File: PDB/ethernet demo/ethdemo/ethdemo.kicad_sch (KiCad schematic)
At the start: 78 parts, among them J1 0826-1X1T-GJ-F, J2 0826-1X1T-GJ-F, Q1 CSD19538Q3AT, U1 STM32H742VGTx, U2 KSZ8863RLLI, U3 TPS23861PWR, Y1 25MHz

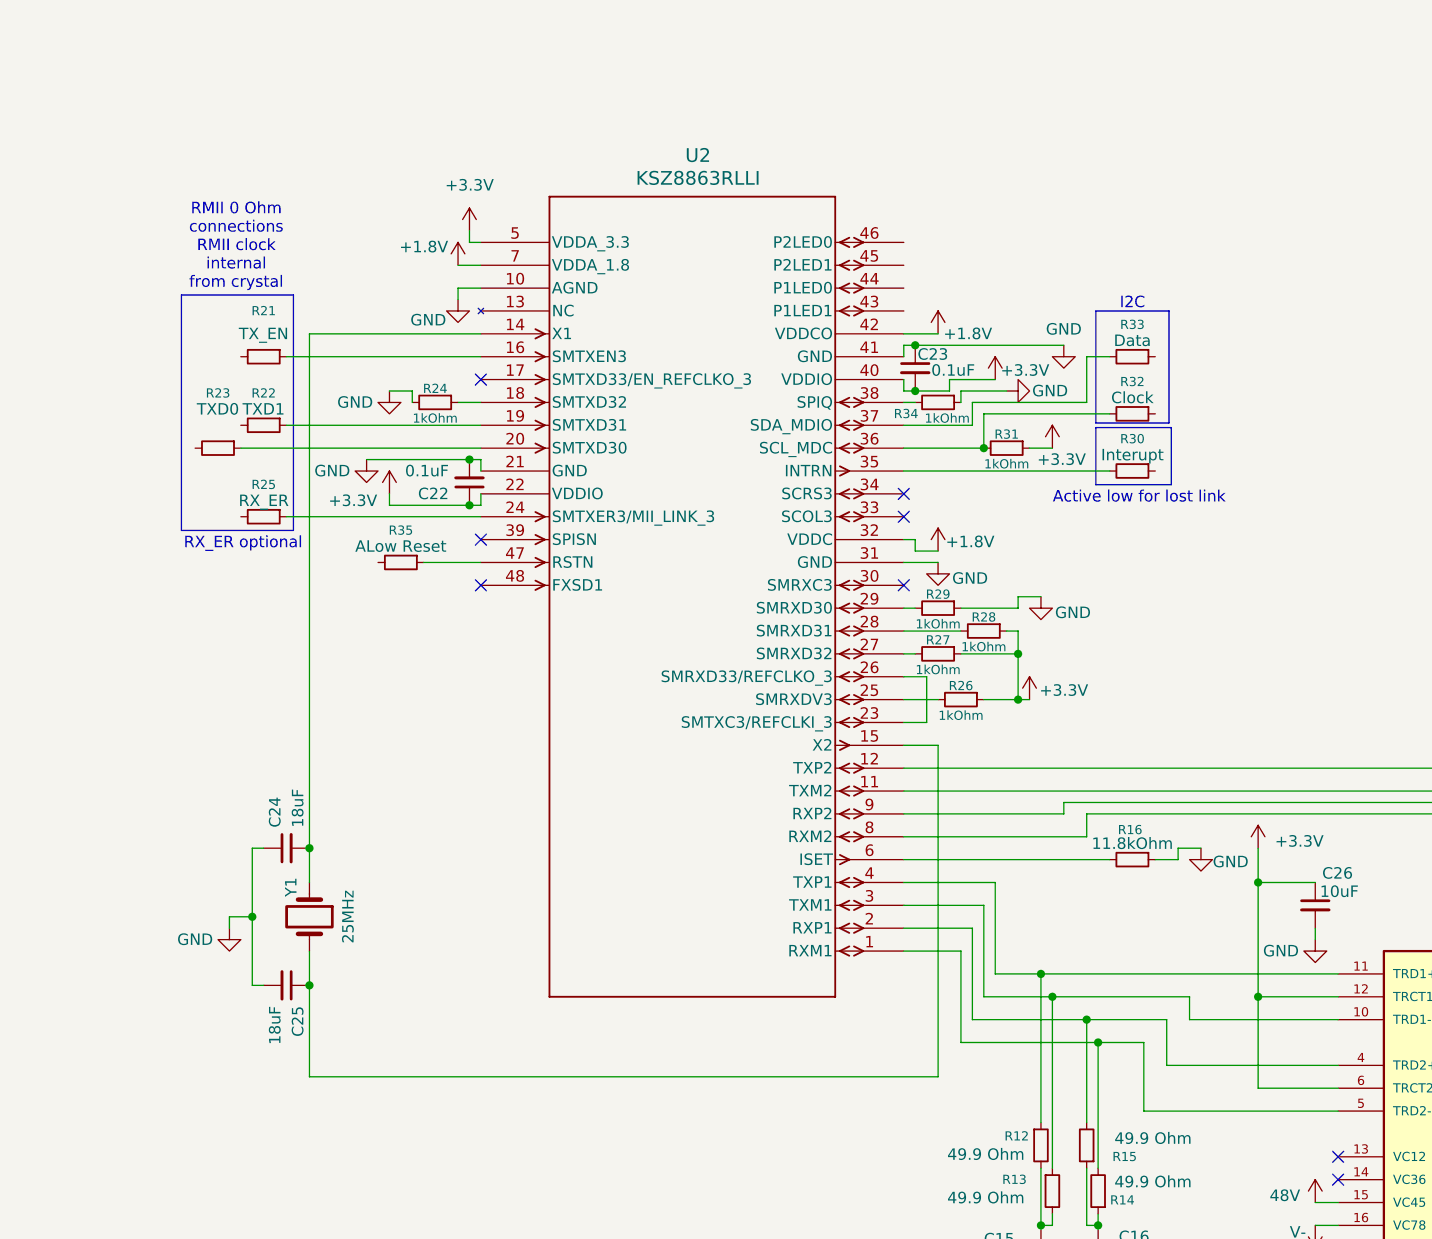
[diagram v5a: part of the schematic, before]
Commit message: Repaired Switch power
Fixed incorrect coupling for power and crystal
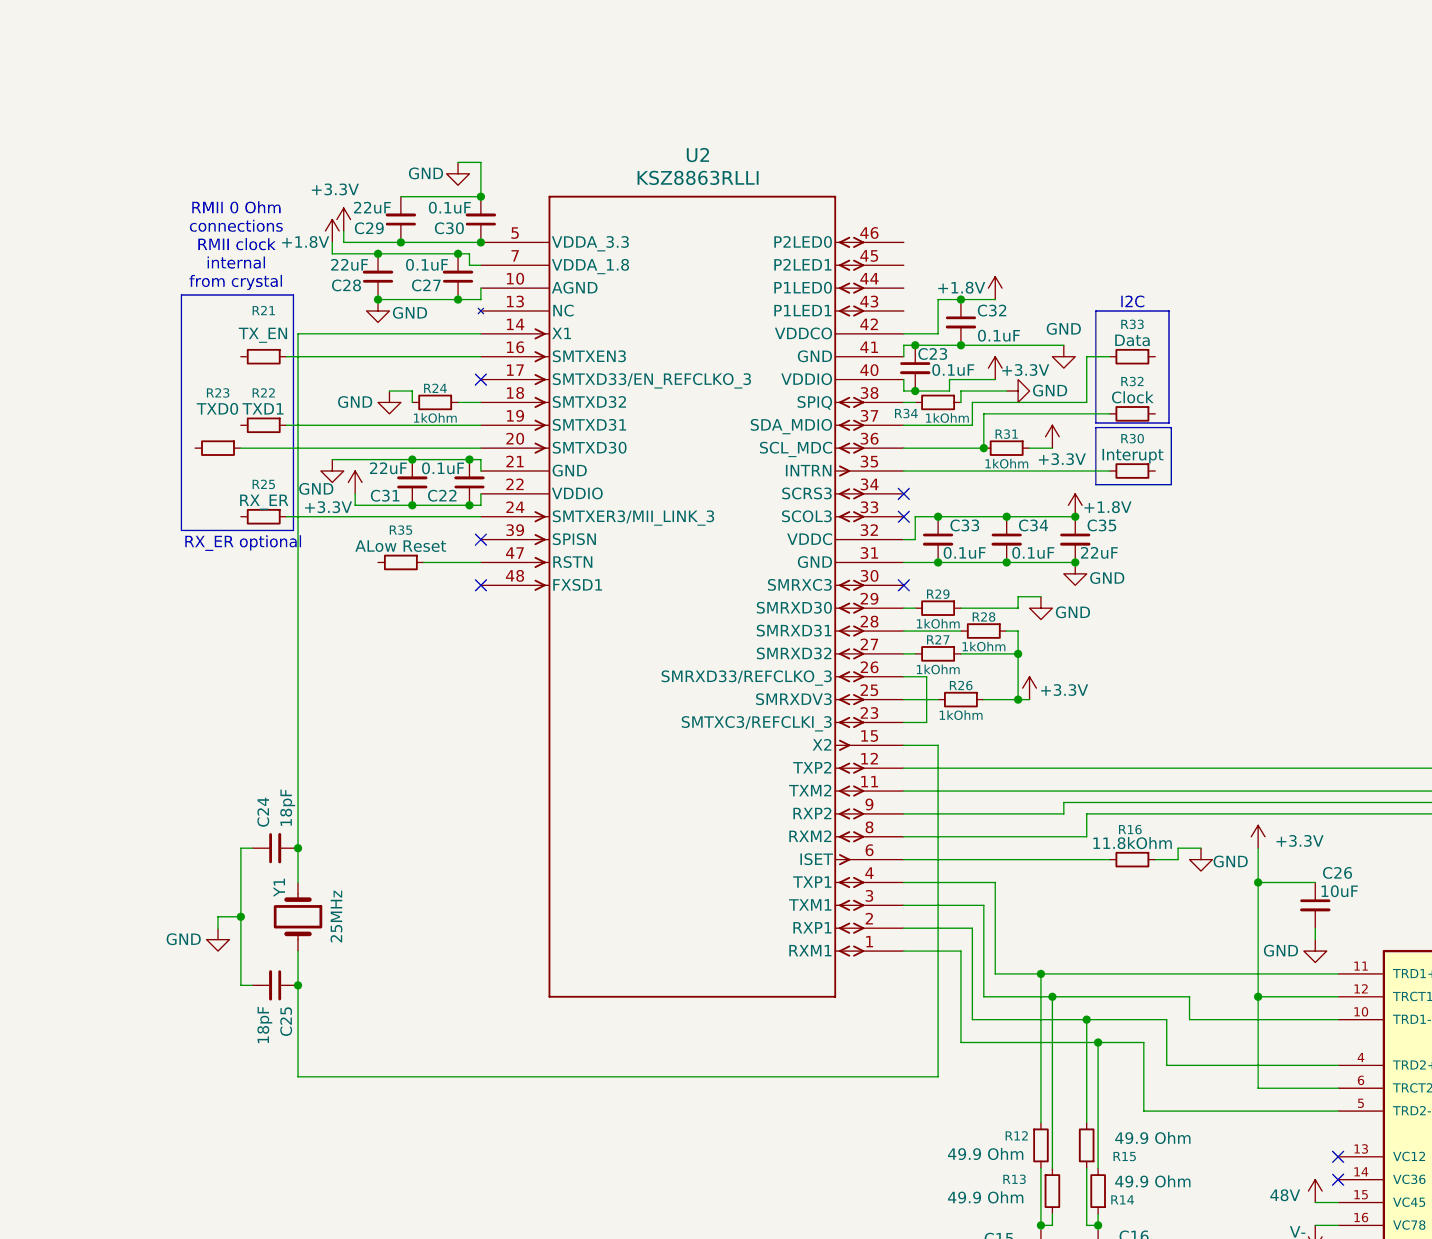
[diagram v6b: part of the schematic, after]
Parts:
- added C27, C30, C32, C33, C34: 0.1uF, symbol Device:C_Small
- added C28, C29, C31, C35: 22uF, symbol Device:C_Small
- C24, C25: value 18uF -> 18pF
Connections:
- net +1.8V: now also C27.2, C28.2, C32.1, C33.1, C34.1, C35.1
- net +3.3V: now also C29.1, C30.1, C31.1
- net GND: now also C27.1, C28.1, C29.2, C30.2, C31.2, C32.2, C33.2, C34.2, C35.2
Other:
- note removed: "Active low for lost link"
- moved on the sheet: C24, C25, Y1

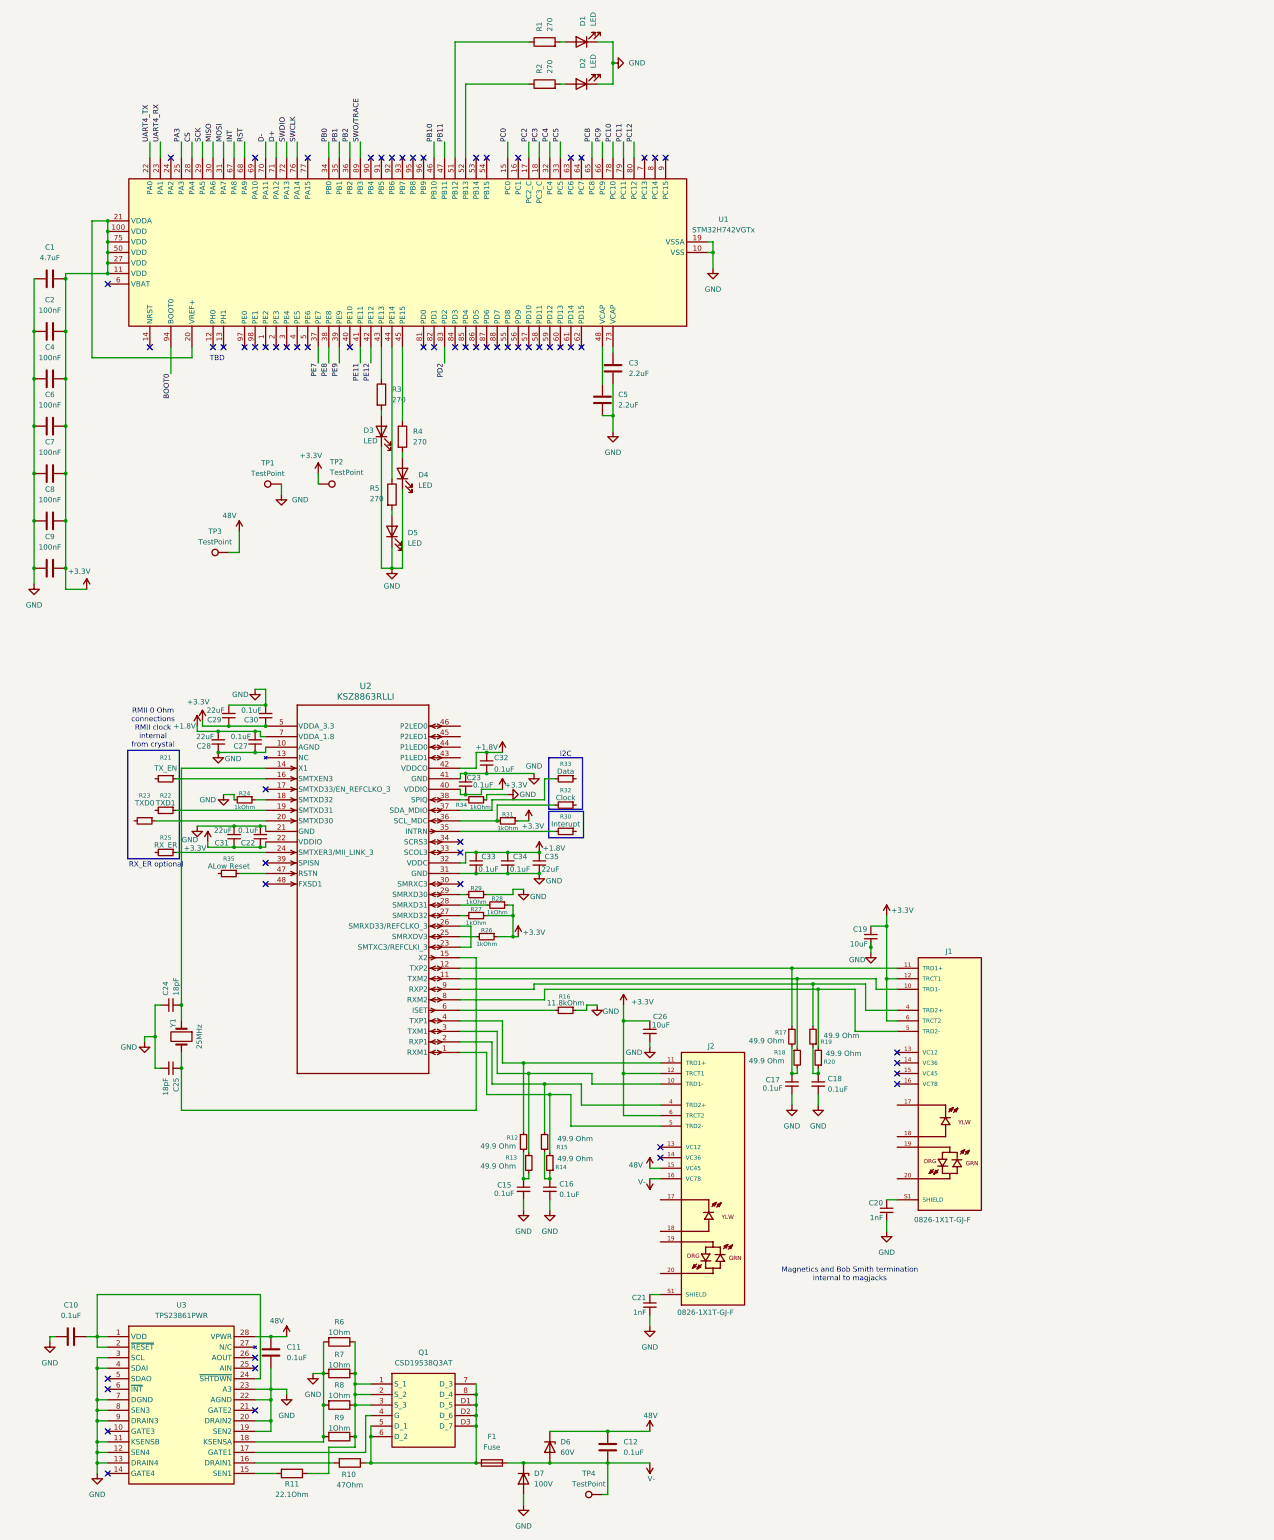
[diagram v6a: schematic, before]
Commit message: fixed clock to mcu standards
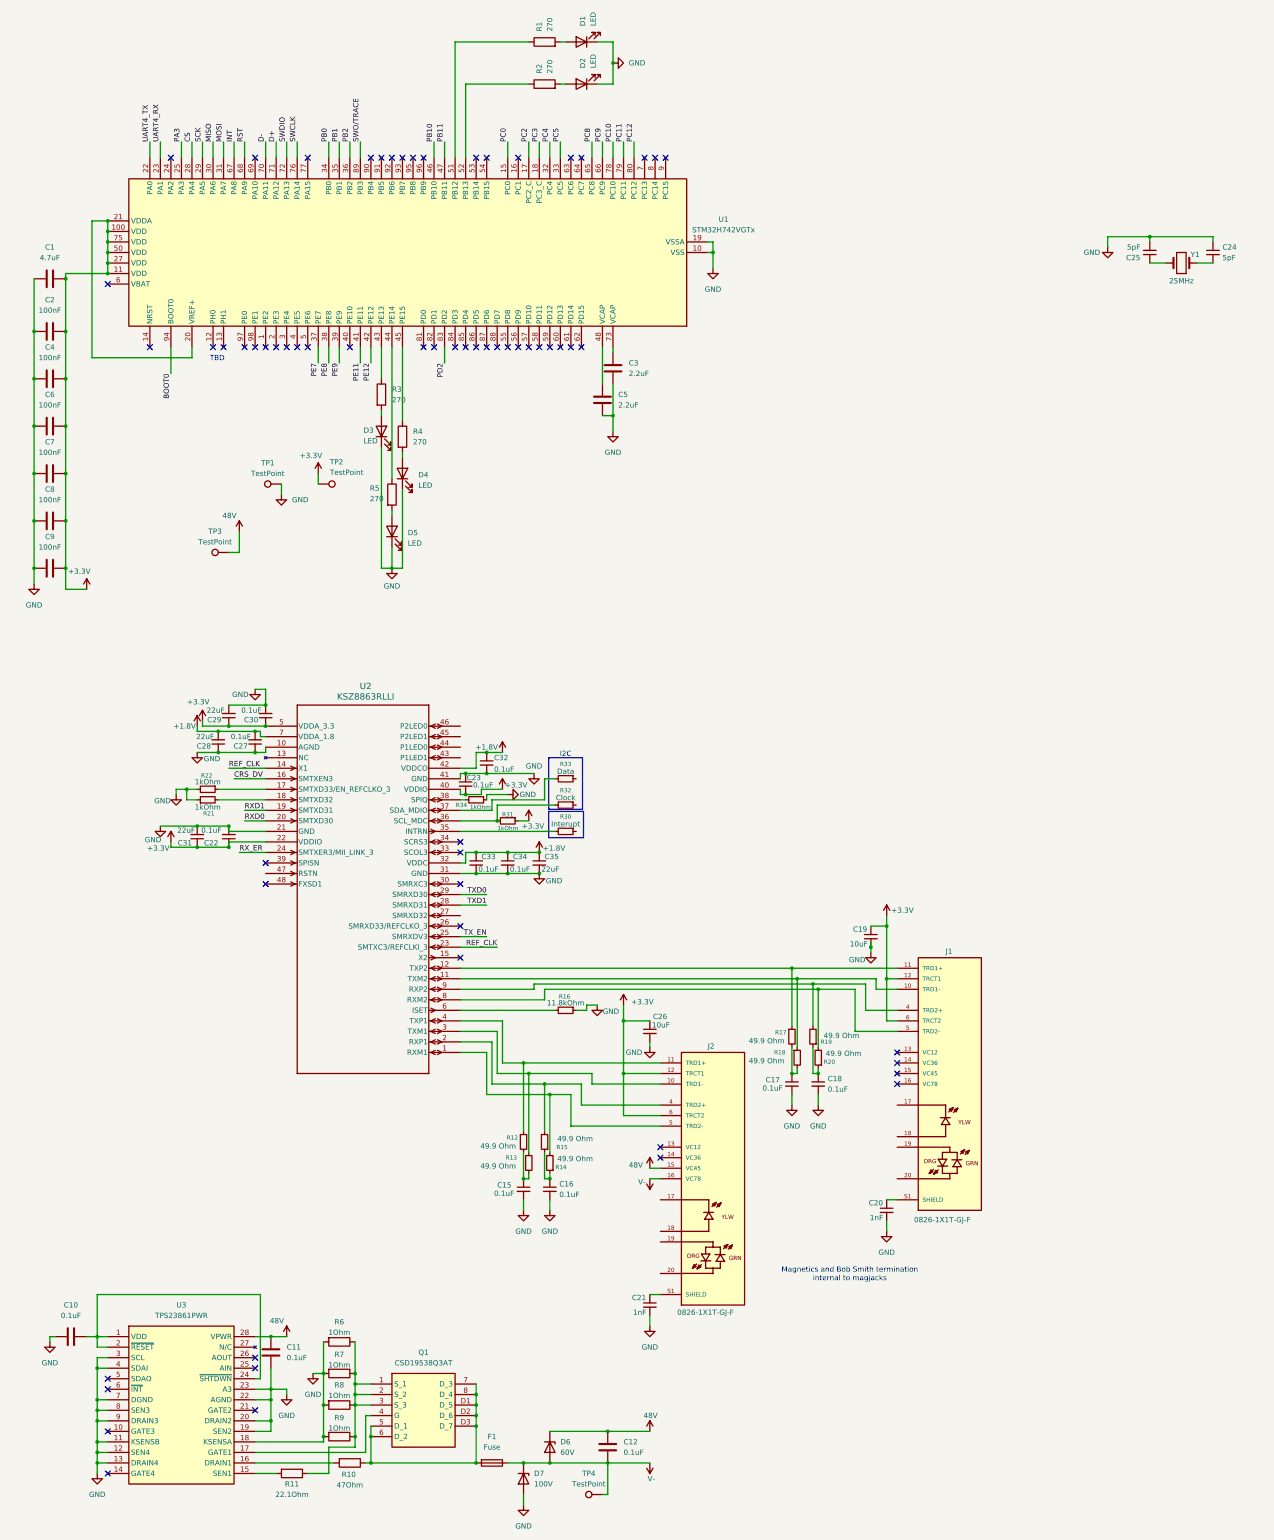
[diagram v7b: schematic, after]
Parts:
- removed R23: TXD0, symbol Device:R_Small
- removed R24, R26, R27, R28, R29: 1kOhm, symbol Device:R_Small
- removed R25: RX_ER, symbol Device:R_Small
- removed R35: ALow Reset, symbol Device:R_Small
- C24, C25: value 18pF -> 5pF
- R21: value TX_EN -> 1kOhm
- R22: value TXD1 -> 1kOhm
- Y1: footprint Crystal:Crystal_SMD_5032-2Pin_5.0x3.2mm -> Crystal:Crystal_SMD_5032-4Pin_5.0x3.2mm
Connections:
- net GND: now also R21.1, R22.2
- net at U2.18 (SMTXD32): now also R21.2
- net at C25.1, Y1.2: no longer U2.15 (X2)
- net CRS_DV: now reaches U2.16 (SMTXEN3)
- net CRS_DV: no longer R21.1
- net TXD0: now reaches U2.29 (SMRXD30)
- net at C24.2, Y1.1: no longer U2.14 (X1)
- net TX_EN: now reaches U2.25 (SMRXDV3)
- net RXD0: now reaches U2.20 (SMTXD30)
- net at U2.17 (SMTXD33/EN_REFCLKO_3): now also R22.1
- net RXD1: now reaches U2.19 (SMTXD31)
- net RXD1: no longer R22.1
- net at U2.26 (SMRXD33/REFCLKO_3): no longer U2.23 (SMTXC3/REFCLKI_3)
- net RX_ER: now reaches U2.24 (SMTXER3/MII_LINK_3)
- net TXD1: now reaches U2.28 (SMRXD31)
- new net REF_CLK: U2.14 (X1), U2.23 (SMTXC3/REFCLKI_3)
- no-connect marks 63 -> 64
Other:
- note removed: "RMII 0 Ohm connections RMII clock internal from crystal"
- note removed: "RX_ER optional"
- moved on the sheet: C22, C24, C25, C31, Y1

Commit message: Demo switch schem
completed instructions form the switch hardware checklist, need to connect I2C on PoE+, I2C switch, and RMII to MCU
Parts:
- removed R32: Clock, symbol Device:R_Small
- removed R33: Data, symbol Device:R_Small
- added C36: 10uF, symbol Device:C_Small
- added D8: 1N4001, Diode_THT:D_DO-41_SOD81_P10.16mm_Horizontal, symbol Diode:1N4001
- added R23, R38, R39, R40, R41: 10kOhm, symbol Device:R_Small
- added R24, R25, R26, R27, R28, R29, R37: 22 Ohm, symbol Device:R_Small
- added R35, R36, R42: 4.7kOhm, symbol Device:R_Small
- added R43, R44, R45, R46: 220 Ohm, symbol Device:R_Small
- added R47, R48, R49, R50: 1kOhm, symbol Device:R_Small
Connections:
- net +3.3V: now also D8.1 (K), R23.2, R35.1, R36.1, R38.1, R39.1, R40.1, R41.1, R43.2, R44.2, R45.2, R46.2, R48.2, R49.2, R50.2
- net CRS_DV: now also R28.1; no longer U2.16 (SMTXEN3)
- net GND: now also C36.1, R42.1, R47.2
- net REF_CLK: now also R27.2; no longer U2.23 (SMTXC3/REFCLKI_3)
- net RXD0: now also R37.2; no longer U2.20 (SMTXD30)
- net RXD1: now also R29.2; no longer U2.19 (SMTXD31)
- net TXD0: now also R24.1; no longer U2.29 (SMRXD30)
- net TXD1: now also R25.2; no longer U2.28 (SMRXD31)
- net TX_EN: now also R26.1; no longer U2.25 (SMRXDV3)
- net Data: now reaches U2.37 (SDA_MDIO)
- net Data: now also R36.2
- net P1LED1: now reaches J1.17
- net P1LED1: now also J2.17, U2.43 (P1LED1), R48.1, R49.1
- net at J1.18: now also R45.1
- net P1LED0: now reaches J1.19
- net P1LED0: now also J2.19, U2.44 (P1LED0), R47.1, R50.1
- net at J1.20: now also R46.1
- net at J2.18: now also R43.1
- net at J2.20: now also R44.1
- net Clock: now reaches R31.2, U2.36 (SCL_MDC)
- net at U2.26 (SMRXD33/REFCLKO_3): now also R39.2
- net at U2.27 (SMRXD32): now also R40.2
- net at R30.2, U2.35 (INTRN): now also R35.2
- net P2LED1: now reaches U2.45 (P2LED1)
- net P2LED0: now reaches U2.46 (P2LED0)
- net at U2.47 (RSTN): now also C36.2, D8.2 (A), R23.1
- net RX_ER: no longer names the net of U2.24 (SMTXER3/MII_LINK_3)
- new net: R29.1, U2.19 (SMTXD31)
- new net: R25.1, R41.2, U2.28 (SMRXD31)
- new net: R26.2, R38.2, U2.25 (SMRXDV3)
- new net: R27.1, U2.23 (SMTXC3/REFCLKI_3)
- new net: R28.2, U2.16 (SMTXEN3)
- new net: R37.1, U2.20 (SMTXD30)
- new net: R24.2, R42.2, U2.29 (SMRXD30)
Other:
- note added: "Change acording to PLL input requirements and external crystal HSC requirements target 10MHZ PLL to 50MHZ for RMII REF_CLK"
- moved on the sheet: C19, C20, C22, C23, C32, J1, R21, R22, R30, R31, R34
